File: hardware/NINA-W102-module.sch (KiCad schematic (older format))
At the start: 4 parts

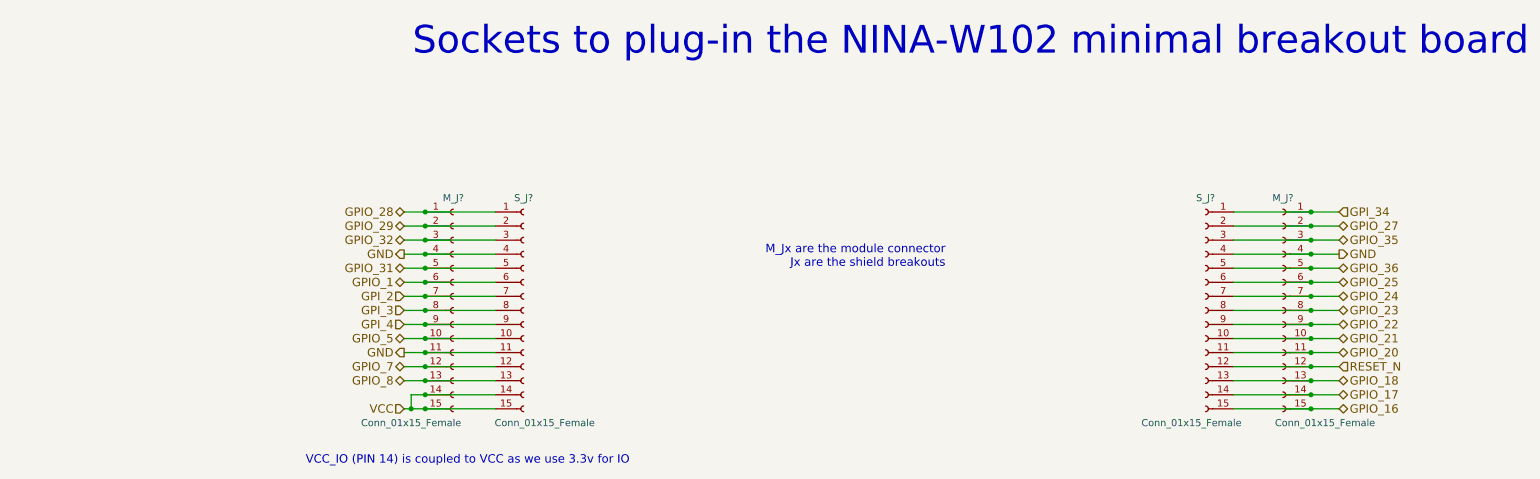
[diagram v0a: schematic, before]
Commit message: Added I2C headers and connected programmer to nina module
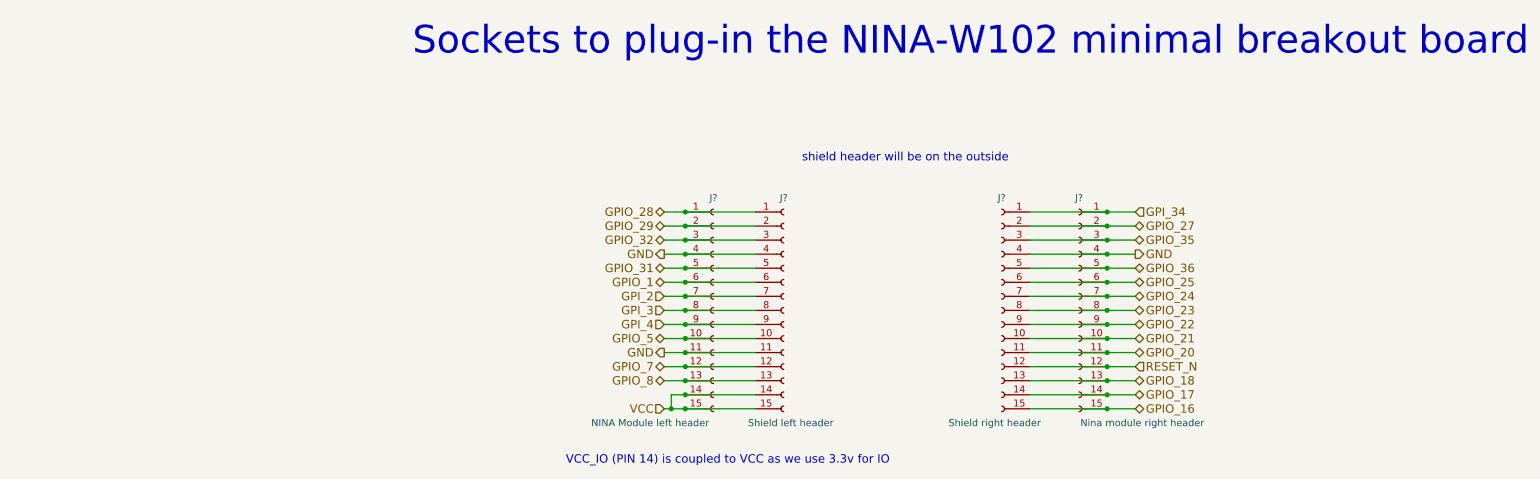
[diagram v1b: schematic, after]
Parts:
- J?: renamed from M_J?; value Conn_01x15_Female -> NINA Module left header
- J?: renamed from M_J?; value Conn_01x15_Female -> Nina module right header
- J?: renamed from S_J?; value Conn_01x15_Female -> Shield left header
- J?: renamed from S_J?; value Conn_01x15_Female -> Shield right header
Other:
- note added: "shield header will be on the outside"
- note removed: "M_Jx are the module connector\nJx are the shield breakouts"
- moved on the sheet: J?

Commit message: added missing sub schema file and comments
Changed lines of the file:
@@
 $EndComp
 Wire Wire Line
-	4150 2750 4300 2750
+	4150 2750 4800 2750
 Wire Wire Line
-	4300 2750 4800 2750
+	4150 2850 4800 2850
 Wire Wire Line
-	4150 2850 4300 2850
+	4150 2950 4800 2950
 Wire Wire Line
-	4300 2850 4800 2850
+	4150 3050 4800 3050
 Wire Wire Line
-	4150 2950 4300 2950
+	4150 3150 4800 3150
 Wire Wire Line
-	4300 2950 4800 2950
+	4150 3250 4800 3250
 Wire Wire Line
-	4150 3050 4300 3050
+	4150 3350 4800 3350
 Wire Wire Line
-	4300 3050 4800 3050
+	4150 3450 4800 3450
 Wire Wire Line
-	4150 3150 4300 3150
+	4150 3550 4800 3550
 Wire Wire Line
-	4300 3150 4800 3150
+	4150 3650 4800 3650
 Wire Wire Line
-	4150 3250 4300 3250
+	4150 3750 4800 3750
 Wire Wire Line
-	4300 3250 4800 3250
+	4150 3850 4800 3850
 Wire Wire Line
-	4150 3350 4300 3350
+	4150 3950 4800 3950
 Wire Wire Line
-	4300 3350 4800 3350
+	4150 4150 4800 4150
 Wire Wire Line
-	4150 3450 4300 3450
-Wire Wire Line
-	4300 3450 4800 3450
-Wire Wire Line
-	4150 3550 4300 3550
-Wire Wire Line
-	4300 3550 4800 3550
-Wire Wire Line
-	4150 3650 4300 3650
-Wire Wire Line
-	4300 3650 4800 3650
-Wire Wire Line
-	4150 3750 4300 3750
-Wire Wire Line
-	4300 3750 4800 3750
-Wire Wire Line
-	4150 3850 4300 3850
-Wire Wire Line
-	4300 3850 4800 3850
-Wire Wire Line
-	4150 3950 4300 3950
-Wire Wire Line
-	4300 3950 4800 3950
-Wire Wire Line
-	4150 4150 4200 4150
-Wire Wire Line
-	4200 4150 4300 4150
-Wire Wire Line
-	4300 4150 4800 4150
-Wire Wire Line
-	4200 4050 4300 4050
-Wire Wire Line
-	4300 4050 4800 4050
+	4200 4050 4800 4050
 Wire Wire Line
 	4200 4050 4200 4150
 Connection ~ 4200 4150
 Wire Wire Line
-	6750 2750 7300 2750
+	6750 2750 7500 2750
 Wire Wire Line
-	7300 2750 7500 2750
+	6750 2850 7500 2850
 Wire Wire Line
-	6750 2850 7300 2850
+	6750 2950 7500 2950
 Wire Wire Line
-	7300 2850 7500 2850
+	6750 3050 7500 3050
 Wire Wire Line
-	6750 2950 7300 2950
+	6750 3150 7500 3150
 Wire Wire Line
-	7300 2950 7500 2950
+	6750 3250 7500 3250
 Wire Wire Line
-	6750 3050 7300 3050
+	6750 3350 7500 3350
 Wire Wire Line
-	7300 3050 7500 3050
+	6750 3450 7500 3450
 Wire Wire Line
-	6750 3150 7300 3150
+	6750 3550 7500 3550
 Wire Wire Line
-	7300 3150 7500 3150
+	6750 3650 7500 3650
 Wire Wire Line
-	6750 3250 7300 3250
+	6750 3750 7500 3750
 Wire Wire Line
-	7300 3250 7500 3250
+	6750 3850 7500 3850
 Wire Wire Line
-	6750 3350 7300 3350
+	6750 3950 7500 3950
 Wire Wire Line
-	7300 3350 7500 3350
+	6750 4050 7500 4050
 Wire Wire Line
-	6750 3450 7300 3450
-Wire Wire Line
-	7300 3450 7500 3450
-Wire Wire Line
-	6750 3550 7300 3550
-Wire Wire Line
-	7300 3550 7500 3550
-Wire Wire Line
-	6750 3650 7300 3650
-Wire Wire Line
-	7300 3650 7500 3650
-Wire Wire Line
-	6750 3750 7300 3750
-Wire Wire Line
-	7300 3750 7500 3750
-Wire Wire Line
-	6750 3850 7300 3850
-Wire Wire Line
-	7300 3850 7500 3850
-Wire Wire Line
-	6750 3950 7300 3950
-Wire Wire Line
-	7300 3950 7500 3950
-Wire Wire Line
-	6750 4050 7300 4050
-Wire Wire Line
-	7300 4050 7500 4050
-Wire Wire Line
-	6750 4150 7300 4150
-Wire Wire Line
-	7300 4150 7500 4150
+	6750 4150 7500 4150
 Connection ~ 4300 2750
 Connection ~ 4300 2850

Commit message: Finished first complete revision for badge carrier board schematic
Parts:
- gave numbers to parts that had none: 4
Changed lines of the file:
@@
 $Descr A4 11693 8268
 encoding utf-8
-Sheet 4 4
+Sheet 2 2
 Title "IoT conference badge - mainboard"
-Date "2018-04-29"
-Rev "0.2.0"
+Date "2018-05-19"
+Rev "0.3.2"
 Comp "MakeZürich (makezurich.ch) & GDG Zürich (gdgzh.ch)"
 Comment1 ""
@@
 $EndDescr
 $Comp
-L Conn_01x15_Female J?
+L Conn_01x15_Female J6
 U 1 1 5AE63E40
 P 4500 3450
-F 0 "J?" H 4500 4250 50  0000 C CNN
+F 0 "J6" H 4500 4250 50  0000 C CNN
 F 1 "NINA Module left header" H 4050 2650 50  0000 C CNN
 F 2 "" H 4500 3450 50  0001 C CNN
@@
 $EndComp
 $Comp
-L Conn_01x15_Female J?
+L Conn_01x15_Female J9
 U 1 1 5AE63E71
 P 7100 3450
-F 0 "J?" H 7100 4250 50  0000 C CNN
+F 0 "J9" H 7100 4250 50  0000 C CNN
 F 1 "Nina module right header" H 6650 2650 50  0000 C CNN
 F 2 "" H 7100 3450 50  0001 C CNN
@@
 Sockets to plug-in the NINA-W102 minimal breakout board
 $Comp
-L Conn_01x15_Female J?
+L Conn_01x15_Female J7
 U 1 1 5AE71527
 P 5000 3450
-F 0 "J?" H 5000 4250 50  0000 C CNN
+F 0 "J7" H 5000 4250 50  0000 C CNN
 F 1 "Shield left header" H 5050 2650 50  0000 C CNN
 F 2 "" H 5000 3450 50  0001 C CNN
@@
 $EndComp
 $Comp
-L Conn_01x15_Female J?
+L Conn_01x15_Female J8
 U 1 1 5AE715D2
 P 6550 3450
-F 0 "J?" H 6550 4250 50  0000 C CNN
+F 0 "J8" H 6550 4250 50  0000 C CNN
 F 1 "Shield right header" H 6600 2650 50  0000 C CNN
 F 2 "" H 6550 3450 50  0001 C CNN
